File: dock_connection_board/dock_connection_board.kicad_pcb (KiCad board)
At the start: 2 copper layers, 33 x 25.4 mm, 14 parts, among them J1 USBO, J2 USBI, J3 CHG, J4 I2CI, J5 AUXI, J6 ANI, J7 I2CO, U1 24LC32

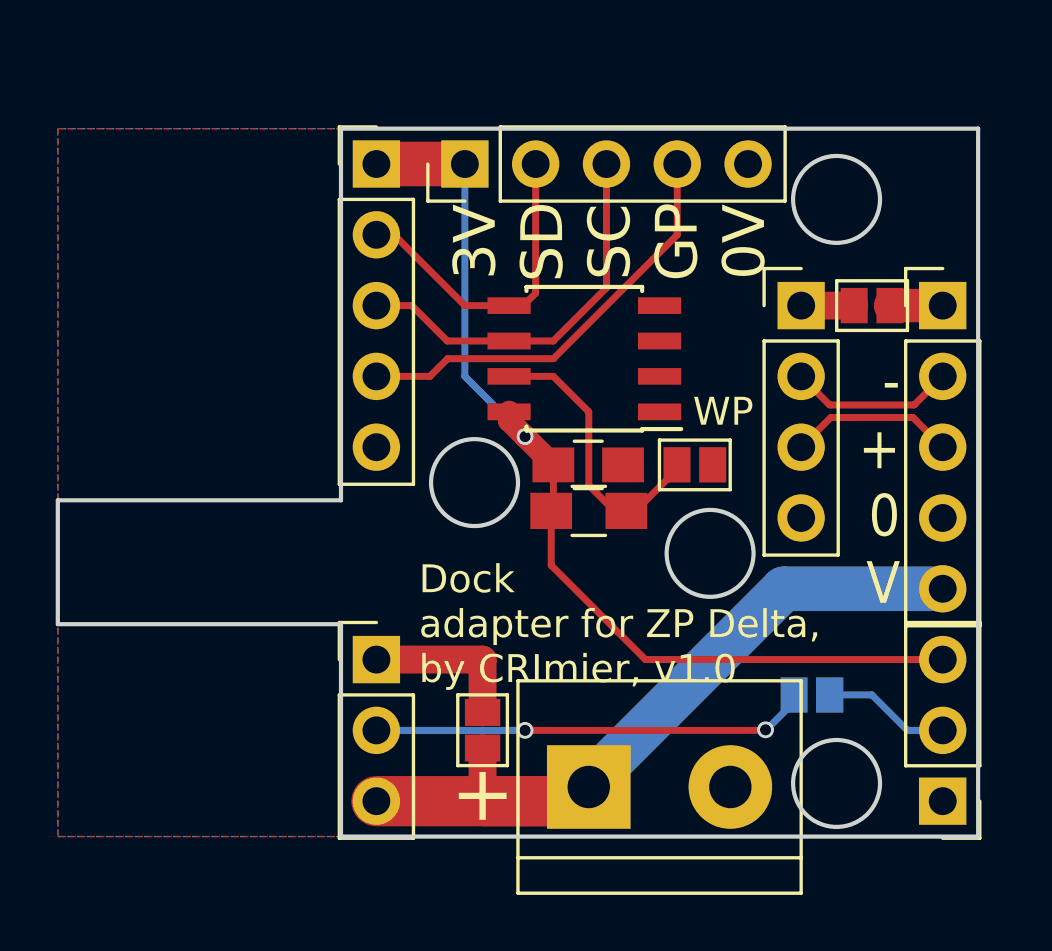
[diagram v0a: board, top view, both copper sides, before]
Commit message: Delta dock board finished
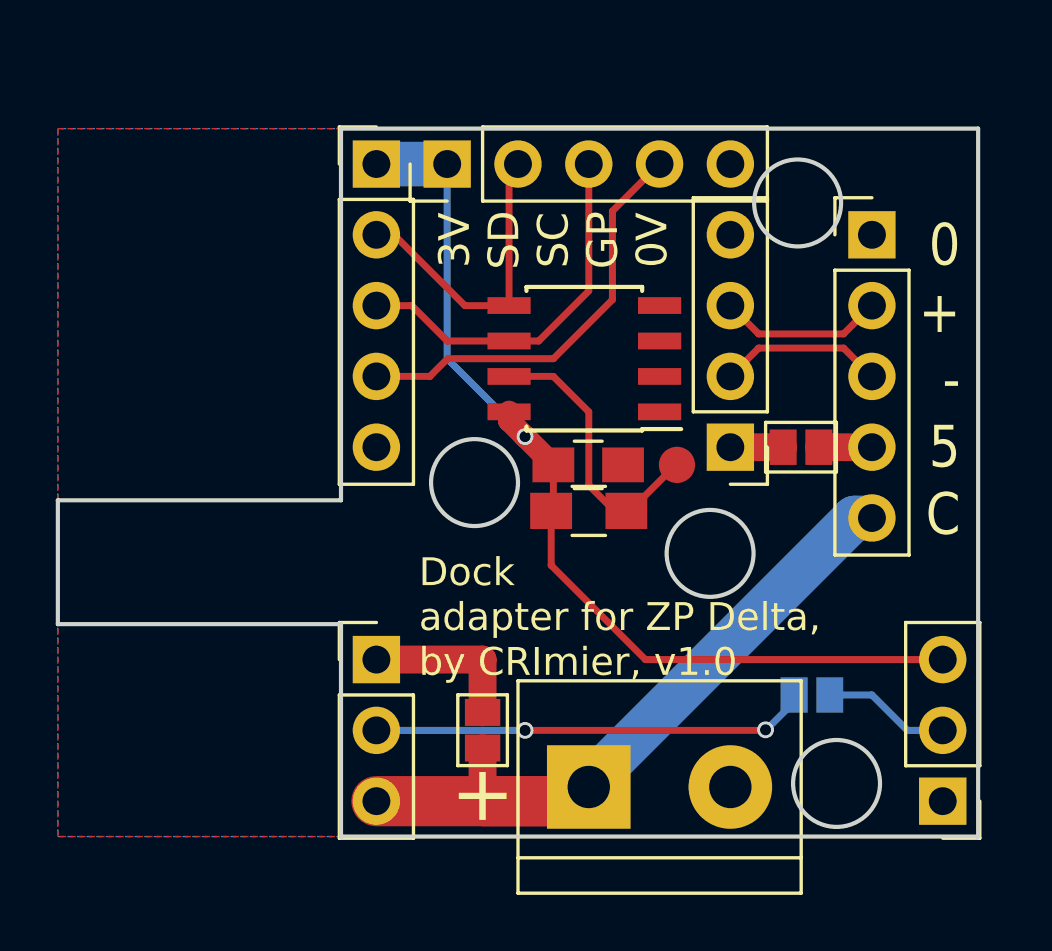
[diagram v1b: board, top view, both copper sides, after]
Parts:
- removed JP4: WP, Connect:GS2
- added TP1: WP, Measurement_Points:Measurement_Point_Round-SMD-Pad_Small, F.Cu at (135.2, 114.9)
- moved JP2 5.68 mm to (139.7, 114.3)
- moved J2 5.68 mm to (137.2, 114.3), turned to 180 degrees
- moved J1 3.59 mm to (142.2, 106.7)
- moved J7 0.64 mm to (127.0, 104.1)
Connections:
- J1 pad 1: Net-(J1-Pad1) -> GND
- J1 pad 2: D- -> D+
- J1 pad 3: D+ -> D-
- J1 pad 4: GND -> Net-(J1-Pad4)
- JP2 pad 1: Net-(J1-Pad1) -> Net-(J1-Pad4)
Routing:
- net Net-(J1-Pad4): track 0.00 -> 1.91 mm
- net Net-(J1-Pad1): track 1.87 -> 0.00 mm
- net CHG: track 29.6 -> 28.1 mm
- net SCL: track 14.0 -> 13.4 mm
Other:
- outline, holes or cut-outs redrawn
- board text added: "0 + - 5 C"
- board text removed: "- + 0 V"

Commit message: Dock board v1.1 - fixing the dock board outline and positioning
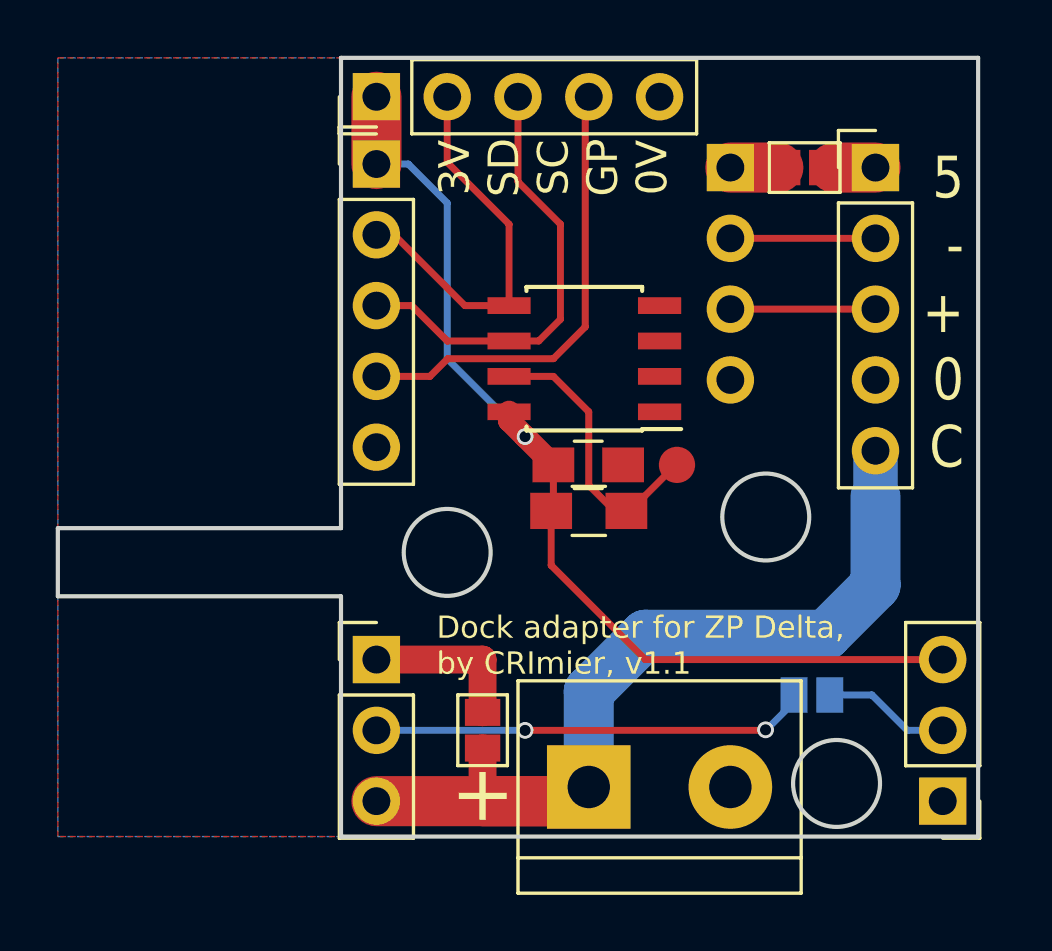
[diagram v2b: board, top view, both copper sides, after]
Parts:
- J2: moved to B.Cu
- moved JP2 10.0 mm to (139.8, 104.3)
- moved J2 10.0 mm to (137.2, 104.3)
- moved J7 3.50 mm to (124.5, 101.7)
- moved J1 2.42 mm to (142.4, 104.3)
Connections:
- J1 pad 1: GND -> Net-(J1-Pad1)
- J1 pad 2: D+ -> D-
- J1 pad 3: D- -> D+
- J1 pad 4: Net-(J1-Pad4) -> GND
- JP2 pad 1: Net-(J1-Pad4) -> Net-(J1-Pad1)
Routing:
- net CHG: track 28.1 -> 34.1 mm
- net SDA: track 11.5 -> 14.7 mm
- net SCL: track 13.4 -> 16.1 mm
- net Net-(J1-Pad4): track 1.91 -> 0.00 mm
- net +3V3: track 35.1 -> 36.7 mm
- net Net-(J1-Pad1): track 0.00 -> 1.48 mm
- net GPIO: track 15.2 -> 16.5 mm
- net D-: track 5.92 -> 5.21 mm
- net D+: track 5.92 -> 5.21 mm
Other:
- board size 33 x 25.4 mm -> 33 x 27.9 mm
- board text added: "5 - + 0 C"
- board text added: "Dock adapter for ZP Delta, by CRImier, v1.1"
- board text removed: "0 + - 5 C"
- board text removed: "Dock adapter for ZP Delta, by CRImier, v1.0"
